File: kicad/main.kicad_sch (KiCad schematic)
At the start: 12 parts, among them U1 74HC00, U2 74HC00

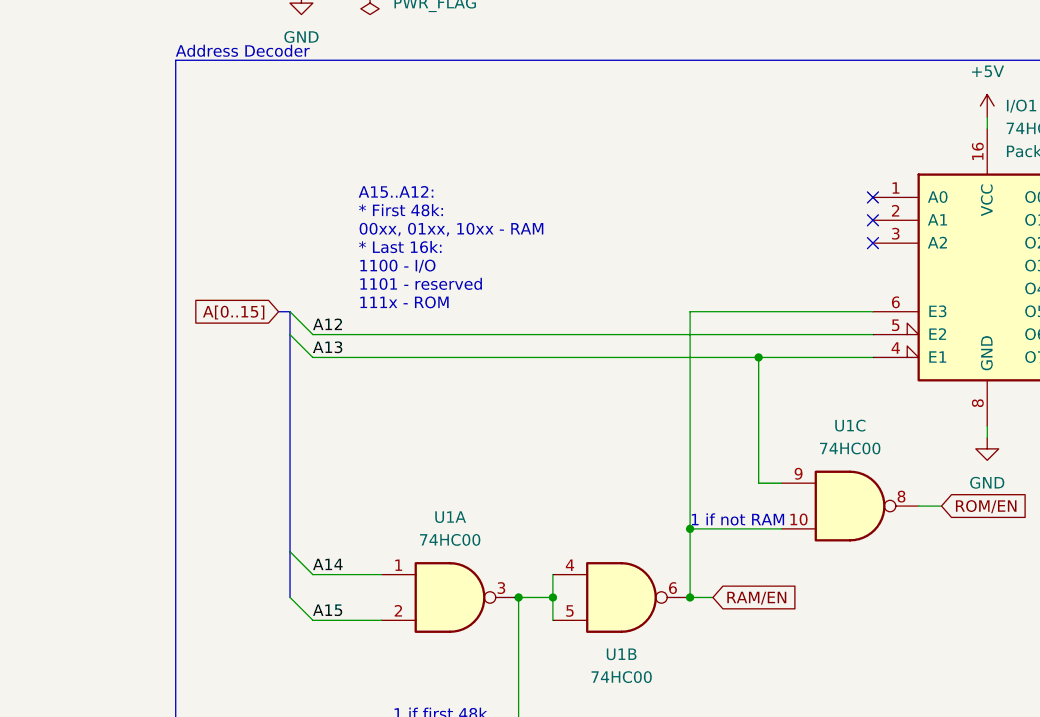
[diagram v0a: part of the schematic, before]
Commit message: Add address lines to 74HC138 (I/O address decoder)
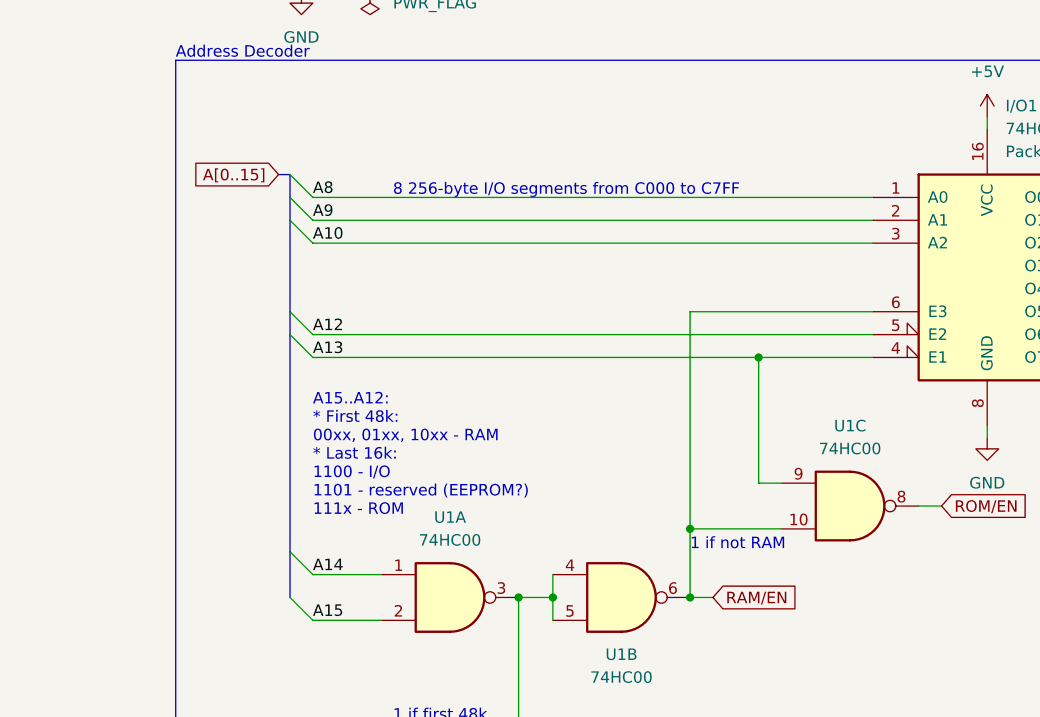
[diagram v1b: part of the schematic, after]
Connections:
- net A10: now also I/O1.3 (A2)
- net A8: now also I/O1.1 (A0)
- net A9: now also I/O1.2 (A1)
- no-connect marks 14 -> 11
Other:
- note added: "8 256-byte I/O segments from C000 to C7FF"
- note added: "A15..A12: * First 48k: 00xx, 01xx, 10xx - RAM * Last 16k: 1100 - I/O 1101 - reserved (EEPROM?) 111x - ROM"
- note removed: "A15..A12: * First 48k: 00xx, 01xx, 10xx - RAM * Last 16k: 1100 - I/O 1101 - reserved 111x - ROM"
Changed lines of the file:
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@@
   (no_connect (at 165.1 138.43))
   (no_connect (at 165.1 140.97))
-  (no_connect (at 139.7 135.89))
   (no_connect (at 60.96 90.17))
-  (no_connect (at 139.7 130.81))
   (no_connect (at 165.1 146.05))
   (no_connect (at 165.1 130.81))
   (no_connect (at 165.1 148.59))
   (no_connect (at 165.1 135.89))
-  (no_connect (at 139.7 133.35))
   (no_connect (at 60.96 85.09))
   (no_connect (at 165.1 133.35))
@@
     (stroke (width 0) (type default) (color 0 0 0 0))
   )
+  (bus_entry (at 74.93 130.81) (size 2.54 2.54)
+    (stroke (width 0) (type default) (color 0 0 0 0))
+  )
   (bus_entry (at 217.17 46.99) (size 2.54 2.54)
     (stroke (width 0) (type default) (color 0 0 0 0))
@@
     (stroke (width 0) (type default) (color 0 0 0 0))
   )
+  (bus_entry (at 74.93 128.27) (size 2.54 2.54)
+    (stroke (width 0) (type default) (color 0 0 0 0))
+  )
   (bus_entry (at 217.17 44.45) (size 2.54 2.54)
     (stroke (width 0) (type default) (color 0 0 0 0))
@@
     (stroke (width 0) (type default) (color 0 0 0 0))
   )
+  (bus_entry (at 74.93 133.35) (size 2.54 2.54)
+    (stroke (width 0) (type default) (color 0 0 0 0))
+  )
   (bus_entry (at 154.94 54.61) (size 2.54 2.54)
     (stroke (width 0) (type default) (color 0 0 0 0))
@@
     (stroke (width 0) (type default) (color 0 0 0 0))
   )
+  (wire (pts (xy 139.7 130.81) (xy 77.47 130.81))
+    (stroke (width 0) (type default) (color 0 0 0 0))
+  )
   (bus (pts (xy 99.06 95.25) (xy 99.06 97.79))
     (stroke (width 0) (type default) (color 0 0 0 0))
@@
     (stroke (width 0) (type default) (color 0 0 0 0))
   )
+  (wire (pts (xy 139.7 133.35) (xy 77.47 133.35))
+    (stroke (width 0) (type default) (color 0 0 0 0))
+  )
   (bus (pts (xy 184.15 64.77) (xy 184.15 62.23))
     (stroke (width 0) (type default) (color 0 0 0 0))
@@
     (stroke (width 0) (type default) (color 0 0 0 0))
   )
-  (bus (pts (xy 73.66 143.51) (xy 74.93 143.51))
+  (bus (pts (xy 73.66 128.27) (xy 74.93 128.27))
     (stroke (width 0) (type default) (color 0 0 0 0))
   )
@@
     (stroke (width 0) (type default) (color 0 0 0 0))
   )
+  (bus (pts (xy 74.93 128.27) (xy 74.93 130.81))
+    (stroke (width 0) (type default) (color 0 0 0 0))
+  )
   (bus (pts (xy 99.06 87.63) (xy 99.06 90.17))
     (stroke (width 0) (type default) (color 0 0 0 0))
@@
     (stroke (width 0) (type default) (color 0 0 0 0))
   )
+  (wire (pts (xy 139.7 135.89) (xy 77.47 135.89))
+    (stroke (width 0) (type default) (color 0 0 0 0))
+  )
   (wire (pts (xy 191.77 74.93) (xy 189.23 74.93))
     (stroke (width 0) (type default) (color 0 0 0 0))
@@
     (stroke (width 0) (type default) (color 0 0 0 0))
   )
+  (bus (pts (xy 74.93 130.81) (xy 74.93 133.35))
+    (stroke (width 0) (type default) (color 0 0 0 0))
+  )
   (wire (pts (xy 91.44 90.17) (xy 96.52 90.17))
     (stroke (width 0) (type default) (color 0 0 0 0))
@@
     (stroke (width 0) (type default) (color 0 0 0 0))
   )
+  (bus (pts (xy 74.93 133.35) (xy 74.93 143.51))
+    (stroke (width 0) (type default) (color 0 0 0 0))
+  )
   (wire (pts (xy 91.44 39.37) (xy 96.52 39.37))
     (stroke (width 0) (type default) (color 0 0 0 0))
@@
     (effects (font (size 1.27 1.27)) (justify left bottom))
   )
-  (text "A15..A12:\n* First 48k:\n00xx, 01xx, 10xx - RAM\n* Last 16k:\n1100 - I/O\n1101 - reserved\n111x - ROM"
-    (at 82.55 143.51 0)
-    (effects (font (size 1.27 1.27)) (justify left bottom))
-  )
-  (text "1 if not RAM" (at 119.38 167.64 0)
+  (text "A15..A12:\n* First 48k:\n00xx, 01xx, 10xx - RAM\n* Last 16k:\n1100 - I/O\n1101 - reserved (EEPROM?)\n111x - ROM"
+    (at 77.47 166.37 0)
+    (effects (font (size 1.27 1.27)) (justify left bottom))
+  )
+  (text "8 256-byte I/O segments from C000 to C7FF" (at 86.36 130.81 0)
+    (effects (font (size 1.27 1.27)) (justify left bottom))
+  )
+  (text "1 if not RAM" (at 119.38 170.18 0)
     (effects (font (size 1.27 1.27)) (justify left bottom))
   )
@@
     (effects (font (size 1.27 1.27)) (justify left bottom))
   )
+  (label "A8" (at 77.47 130.81 0)
+    (effects (font (size 1.27 1.27)) (justify left bottom))
+  )
   (label "A7" (at 120.65 59.69 0)
     (effects (font (size 1.27 1.27)) (justify left bottom))
@@
     (effects (font (size 1.27 1.27)) (justify left bottom))
   )
+  (label "A9" (at 77.47 133.35 0)
+    (effects (font (size 1.27 1.27)) (justify left bottom))
+  )
   (label "D0" (at 151.13 41.91 0)
     (effects (font (size 1.27 1.27)) (justify left bottom))
@@
   )
   (label "D0" (at 92.71 80.01 0)
+    (effects (font (size 1.27 1.27)) (justify left bottom))
+  )
+  (label "A10" (at 77.47 135.89 0)
     (effects (font (size 1.27 1.27)) (justify left bottom))
   )
@@
     )
   )
-  (global_label "A[0..15]" (shape input) (at 73.66 143.51 180) (fields_autoplaced)
+  (global_label "A[0..15]" (shape input) (at 73.66 128.27 180) (fields_autoplaced)
     (effects (font (size 1.27 1.27)) (justify right))
-    (property "Intersheet References" "${INTERSHEET_REFS}" (id 0) (at 63.6269 143.4306 0)
+    (property "Intersheet References" "${INTERSHEET_REFS}" (id 0) (at 63.6269 128.1906 0)
       (effects (font (size 1.27 1.27)) (justify right) hide)
     )

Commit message: V6
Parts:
- removed R6: 3K3, Resistor_THT:R_Axial_DIN0204_L3.6mm_D1.6mm_P7.62mm_Horizontal, symbol Device:R
- removed RAM1: AS6C4008-55PCN, Package_DIP:DIP-32_W15.24mm, symbol Memory_RAM:AS6C4008-55PCN
- removed unit 4 of U1
- added unit 5 of ADDR1
- added C1, C3: 10uF 50V, Capacitor_THT:C_Disc_D3.0mm_W2.0mm_P2.50mm, symbol Device:C
- added C2, C4, C5, C6, C7, C8, C9: 0.1uF 50V, Capacitor_THT:C_Disc_D3.0mm_W2.0mm_P2.50mm, symbol Device:C
- added J1: Jack-DC, Connector_BarrelJack:BarrelJack_GCT_DCJ200-10-A_Horizontal, symbol Connector:Jack-DC
- added J2: LCD_Conn, Connector_PinHeader_2.54mm:PinHeader_1x16_P2.54mm_Vertical, symbol Connector:Conn_01x16_Male
- added J3: VIA_Conn, Connector_PinHeader_2.54mm:PinHeader_1x22_P2.54mm_Vertical, symbol Connector:Conn_01x22_Male
- added JP1: Clock_Mode, Connector_PinHeader_2.54mm:PinHeader_1x03_P2.54mm_Vertical, symbol Jumper:Jumper_3_Open
- added RAM1: AS6C62256-55RCN, Package_DIP:DIP-28_W15.24mm, symbol Memory_RAM:CY62256-70PC
- added REG1: TSC 1-2450, Package_TO_SOT_THT:TO-220-3_Vertical, symbol Regulator_Linear:LM7805_TO220
- added RES1, STEP1: DS1813-10, Package_TO_SOT_THT:TO-92_Inline, symbol ds1813:DS1813-5+
- added RV1: 10K, Potentiometer_THT:Potentiometer_Bourns_3296Y_Vertical, symbol Device:R_Potentiometer
- added unit 5 of RW1
- added SW1: Step, Button_Switch_THT:SW_PUSH_6mm_H5mm, symbol Switch:SW_Push
- added SW2: Reset, Button_Switch_THT:SW_PUSH_6mm_H5mm, symbol Switch:SW_Push
- added VIA1: W65C22N6TPG-14, Package_DIP:DIP-40_W15.24mm, symbol 65xx:W65C22NxP
- added X1: 1 MHz, Oscillator:Oscillator_DIP-14, symbol Oscillator:CXO_DIP14
- CPU1: value W65C02SxP -> W65C02S6TPG-14
- IO1: renamed from I/O1; footprint Package_DIP:DIP-16_W7.62mm_LongPads -> Package_DIP:DIP-16_W7.62mm
- renumbered U1 to ADDR1, EPROM1 to ROM1, U2 to RW1
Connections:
- net /RD is gone; now on net ~{RD}: RW1.8
- net +5V: now also R5.1, ADDR1.14 (VCC), C2.1, C3.1, C4.1, C5.1, C6.1, C7.1, C8.1, C9.1, J2.15 (Pin_15), J2.2 (Pin_2), J3.21 (Pin_21), RAM1.28 (VCC), REG1.3 (VO), RES1.2 (VCC), RV1.3, RW1.14 (VCC), STEP1.2 (VCC), VIA1.20 (VCC), VIA1.24 (CS1), X1.14 (Vcc); no longer R5.2
- net GND: now also ADDR1.7 (GND), C1.2, C2.2, C3.2, C4.2, C5.2, C6.2, C7.2, C8.2, C9.2, J1.2, J2.1 (Pin_1), J2.16 (Pin_16), J3.22 (Pin_22), RAM1.14 (GND), REG1.2 (GND), RES1.3 (GND), RV1.1, RW1.7 (GND), STEP1.3 (GND), SW1.2, SW2.2, VIA1.1 (VSS), X1.7 (GND)
- net Ф2: now also VIA1.25 (ϕ2)
- net at CPU1.38 (~{SO}): now also R5.2; no longer R5.1
- net ~{IRQ}: now reaches CPU1.4 (~{IRQ}), R1.2
- net ~{IRQ}: now also VIA1.21 (~{IRQ})
- net ~{RD}: now reaches ROM1.22 (~{OE})
- net ~{RD}: now also RAM1.22 (~{OE})
- net VIA~{EN}: now reaches IO1.14 (O1)
- net VIA~{EN}: now also VIA1.23 (~{CS2})
- net LCD~{EN}: now reaches IO1.15 (O0)
- net LCD~{EN}: now also J2.6 (Pin_6)
- net A0 renamed A_{0}
- net A_{0}: now also J2.4 (Pin_4), RAM1.10 (A0), VIA1.38 (RS0)
- net A1 renamed A_{1}
- net A_{1}: now also RAM1.9 (A1), VIA1.37 (RS1)
- net A10 renamed A_{10}
- net A_{10}: now also RAM1.21 (A10)
- net A11 renamed A_{11}
- net A_{11}: now also RAM1.23 (A11)
- net A12 renamed A_{12}
- net A_{12}: now also RAM1.2 (A12)
- net A13 renamed A_{13}
- net A_{13}: now also RAM1.26 (A13)
- net A14 renamed A_{14}
- net A_{14}: now also RAM1.1 (A14)
- net A15 renamed A_{15}
- net A2 renamed A_{2}
- net A_{2}: now also RAM1.8 (A2), VIA1.36 (RS2)
- net A3 renamed A_{3}
- net A_{3}: now also RAM1.7 (A3), VIA1.35 (RS3)
- net A4 renamed A_{4}
- net A_{4}: now also RAM1.6 (A4)
- net A5 renamed A_{5}
- net A_{5}: now also RAM1.5 (A5)
- net A6 renamed A_{6}
- net A_{6}: now also RAM1.4 (A6)
- net A7 renamed A_{7}
- net A_{7}: now also RAM1.3 (A7)
- net A8 renamed A_{8}
- net A_{8}: now also RAM1.25 (A8)
- net A9 renamed A_{9}
- net A_{9}: now also RAM1.24 (A9)
- net CLK (TODO): no longer names the net of CPU1.3 (ϕ1)
- net CLK (TODO): no longer CPU1.37 (ϕ0)
- net D0 renamed D_{0}
- net D_{0}: now also J2.7 (Pin_7), RAM1.11 (Q0), VIA1.33 (D0)
- net D1 renamed D_{1}
- net D_{1}: now also J2.8 (Pin_8), RAM1.12 (Q1), VIA1.32 (D1)
- net D2 renamed D_{2}
- net D_{2}: now also J2.9 (Pin_9), RAM1.13 (Q2), VIA1.31 (D2)
- net D3 renamed D_{3}
- net D_{3}: now also J2.10 (Pin_10), RAM1.15 (Q3), VIA1.30 (D3)
- net D4 renamed D_{4}
- net D_{4}: now also J2.11 (Pin_11), RAM1.16 (Q4), VIA1.29 (D4)
- net D5 renamed D_{5}
- net D_{5}: now also J2.12 (Pin_12), RAM1.17 (Q5), VIA1.28 (D5)
- net D6 renamed D_{6}
- net D_{6}: now also J2.13 (Pin_13), RAM1.18 (Q6), VIA1.27 (D6)
- net D7 renamed D_{7}
- net D_{7}: now also J2.14 (Pin_14), RAM1.19 (Q7), VIA1.26 (D7)
- net RAM/EN renamed RAM~{EN}
- net RAM~{EN}: now also RAM1.20 (~{CS})
- net RES (TODO) renamed ~{RES}
- net ~{RES}: now also RES1.1 (~{RST}), SW2.1, VIA1.34 (~{RES})
- net ROM/EN renamed ROM~{EN}
- net R/W renamed R~{W}
- net R~{W}: now also VIA1.22 (R/~{W})
- net /WD renamed ~{WD}
- net ~{WD}: now also J2.5 (Pin_5), RAM1.27 (~{WE})
- new net: CPU1.37 (ϕ0), JP1.2 (C)
- new net: J2.3 (Pin_3), RV1.2
- new net: J3.1 (Pin_1), VIA1.2 (PA0)
- new net: J3.10 (Pin_10), VIA1.39 (CA2)
- new net: J3.11 (Pin_11), VIA1.10 (PB0)
- new net: J3.12 (Pin_12), VIA1.11 (PB1)
- new net: J3.13 (Pin_13), VIA1.12 (PB2)
- new net: J3.14 (Pin_14), VIA1.13 (PB3)
- new net: J3.15 (Pin_15), VIA1.14 (PB4)
- new net: J3.16 (Pin_16), VIA1.15 (PB5)
- new net: J3.17 (Pin_17), VIA1.16 (PB6)
- new net: J3.18 (Pin_18), VIA1.17 (PB7)
- new net: J3.19 (Pin_19), VIA1.18 (CB1)
- new net: J3.2 (Pin_2), VIA1.3 (PA1)
- new net: J3.20 (Pin_20), VIA1.19 (CB2)
- new net: J3.3 (Pin_3), VIA1.4 (PA2)
- new net: J3.4 (Pin_4), VIA1.5 (PA3)
- new net: J3.5 (Pin_5), VIA1.6 (PA4)
- new net: J3.6 (Pin_6), VIA1.7 (PA5)
- new net: J3.7 (Pin_7), VIA1.8 (PA6)
- new net: J3.8 (Pin_8), VIA1.9 (PA7)
- new net: J3.9 (Pin_9), VIA1.40 (CA1)
- new net: C1.1, J1.1, REG1.1 (VI)
- new net CLK: JP1.3 (B), X1.8 (OUT)
- new net STEP: JP1.1 (A), STEP1.1 (~{RST}), SW1.1
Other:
- note added: "$C000-$C0FF"
- note added: "$C100-$C1FF"
- note added: "* I use 32Kx8 SRAM for this prototype since I don't have 128Kx8."
- note added: "A15..A12: * First 48k: 00xx, 01xx, 10xx - RAM ($0000-$BFFF) * Last 16k: 1100 - IO ($C000-$CFFF) 1101 - reserved ($D000-$DFFF - EEPROM?) 111x - ROM ($E000-$FFFF)"
- note added: "Clock & Reset"
- note added: "Generic IO"
- note added: "LCD Connector"
- note added: "Power"
- note removed: "A15..A12: * First 48k: 00xx, 01xx, 10xx - RAM * Last 16k: 1100 - I/O 1101 - reserved (EEPROM?) 111x - ROM"
- note removed: "Prevent accidental writes to ROM"
- company: (none) -> Andrew Dunai
- title: (none) -> 6502 SBC
- moved on the sheet: ADDR1A, ADDR1B, ADDR1C, CPU1, IO1, R2, R3, R4, R5, ROM1, RW1A, RW1B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

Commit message: Final PCB layout (<10*10 cm)
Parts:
- removed C6: 0.1uF 50V, Capacitor_THT:C_Disc_D3.0mm_W2.0mm_P2.50mm, symbol Device:C
- removed J2: LCD_Conn, Connector_PinHeader_2.54mm:PinHeader_1x16_P2.54mm_Vertical, symbol Connector:Conn_01x16_Male
- removed J3: VIA_Conn, Connector_PinHeader_2.54mm:PinHeader_1x22_P2.54mm_Vertical, symbol Connector:Conn_01x22_Male
- removed RAM1: AS6C62256-55RCN, Package_DIP:DIP-28_W15.24mm, symbol Memory_RAM:CY62256-70PC
- added unit 4 of ADDR1
- added C4: 0.1uF, Capacitor_THT:C_Disc_D3.0mm_W2.0mm_P2.50mm, symbol Device:C
- added J2: LCD_Out, Connector_PinHeader_2.54mm:PinHeader_1x14_P2.54mm_Vertical, symbol Connector:Conn_01x14_Male
- added J3: LCD_Light, Connector_PinHeader_2.54mm:PinHeader_1x02_P2.54mm_Vertical, symbol Connector:Conn_01x02_Male
- added J4: VIA_A, Connector_PinHeader_2.54mm:PinHeader_2x05_P2.54mm_Vertical, symbol Connector:Conn_01x10_Male
- added J5: VIA_B, Connector_PinHeader_2.54mm:PinHeader_2x05_P2.54mm_Vertical, symbol Connector:Conn_01x10_Male
- added J6: VIA_Power, Connector_PinHeader_2.54mm:PinHeader_1x02_P2.54mm_Vertical, symbol Connector:Conn_01x02_Male
- added RAM1: AS6C4008, Package_DIP:DIP-32_W15.24mm, symbol Memory_RAM:AS6C4008-55PCN
- added unit 4 of RW1
- C1: renamed from C2; value 0.1uF 50V -> 0.1uF
- C2: renamed from C1; value 10uF 50V -> 10uF
- C3: value 10uF 50V -> 10uF
- C5: renamed from C4; value 0.1uF 50V -> 0.1uF
- C6: renamed from C5; value 0.1uF 50V -> 0.1uF
- C7, C8, C9: value 0.1uF 50V -> 0.1uF
- CPU1: value W65C02S6TPG-14 -> W65C02S6TPG
- RES1, STEP1: value DS1813-10 -> DS1813
- ROM1: value W27C512-45Z -> W27C512; footprint Package_DIP:DIP-28_W15.24mm -> Socket:DIP_Socket-28_W11.9_W12.7_W15.24_W17.78_W18.5_3M_228-1277-00-0602J
- VIA1: value W65C22N6TPG-14 -> W65C22N6TPG
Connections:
- net +5V: now also C4.1, J2.2 (Pin_2), J3.2 (Pin_2), J6.2 (Pin_2), RAM1.1 (A18), RAM1.2 (A16), RAM1.30 (A17), RAM1.32 (VCC)
- net A_{0}: now also J2.4 (Pin_4), RAM1.12 (A0)
- net A_{10}: now also RAM1.23 (A10)
- net A_{11}: now also RAM1.25 (A11)
- net A_{12}: now also RAM1.4 (A12)
- net A_{13}: now also RAM1.28 (A13)
- net A_{14}: now also RAM1.3 (A14)
- net A_{15}: now also RAM1.31 (A15)
- net A_{1}: now also RAM1.11 (A1)
- net A_{2}: now also RAM1.10 (A2)
- net A_{3}: now also RAM1.9 (A3)
- net A_{4}: now also RAM1.8 (A4)
- net A_{5}: now also RAM1.7 (A5)
- net A_{6}: now also RAM1.6 (A6)
- net A_{7}: now also RAM1.5 (A7)
- net A_{8}: now also RAM1.27 (A8)
- net A_{9}: now also RAM1.26 (A9)
- net D_{0}: now also J2.7 (Pin_7), RAM1.13 (DQ0)
- net D_{1}: now also J2.8 (Pin_8), RAM1.14 (DQ1)
- net D_{2}: now also J2.9 (Pin_9), RAM1.15 (DQ2)
- net D_{3}: now also J2.10 (Pin_10), RAM1.17 (DQ3)
- net D_{4}: now also J2.11 (Pin_11), RAM1.18 (DQ4)
- net D_{5}: now also J2.12 (Pin_12), RAM1.19 (DQ5)
- net D_{6}: now also J2.13 (Pin_13), RAM1.20 (DQ6)
- net D_{7}: now also J2.14 (Pin_14), RAM1.21 (DQ7)
- net GND: now also C4.2, J2.1 (Pin_1), J3.1 (Pin_1), J6.1 (Pin_1), RAM1.16 (VSS)
- net LCD~{EN}: now also J2.6 (Pin_6)
- net RAM~{EN}: now also RAM1.22 (CE#)
- net ~{RD}: now also RAM1.24 (OE#)
- net ~{WD}: now also J2.5 (Pin_5), RAM1.29 (WE#)
- net at RV1.2: now also J2.3 (Pin_3)
- net at VIA1.2 (PA0): now also J4.1 (Pin_1)
- net at VIA1.39 (CA2): now also J4.10 (Pin_10)
- net at VIA1.10 (PB0): now also J5.1 (Pin_1)
- net at VIA1.11 (PB1): now also J5.2 (Pin_2)
- net at VIA1.12 (PB2): now also J5.3 (Pin_3)
- net at VIA1.13 (PB3): now also J5.4 (Pin_4)
- net at VIA1.14 (PB4): now also J5.5 (Pin_5)
- net at VIA1.15 (PB5): now also J5.6 (Pin_6)
- net at VIA1.16 (PB6): now also J5.7 (Pin_7)
- net at VIA1.17 (PB7): now also J5.8 (Pin_8)
- net at VIA1.18 (CB1): now also J5.9 (Pin_9)
- net at VIA1.3 (PA1): now also J4.2 (Pin_2)
- net at VIA1.19 (CB2): now also J5.10 (Pin_10)
- net at VIA1.4 (PA2): now also J4.3 (Pin_3)
- net at VIA1.5 (PA3): now also J4.4 (Pin_4)
- net at VIA1.6 (PA4): now also J4.5 (Pin_5)
- net at VIA1.7 (PA5): now also J4.6 (Pin_6)
- net at VIA1.8 (PA6): now also J4.7 (Pin_7)
- net at VIA1.9 (PA7): now also J4.8 (Pin_8)
- net at VIA1.40 (CA1): now also J4.9 (Pin_9)
- no-connect marks 11 -> 17
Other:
- note added: "Compatible with 1008, 2008, & 4008"
- note removed: "* I use 32Kx8 SRAM for this prototype since I don't have 128Kx8."
